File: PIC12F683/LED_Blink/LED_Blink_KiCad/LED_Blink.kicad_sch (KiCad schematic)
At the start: 3 parts, among them U1 PIC12F683-xP

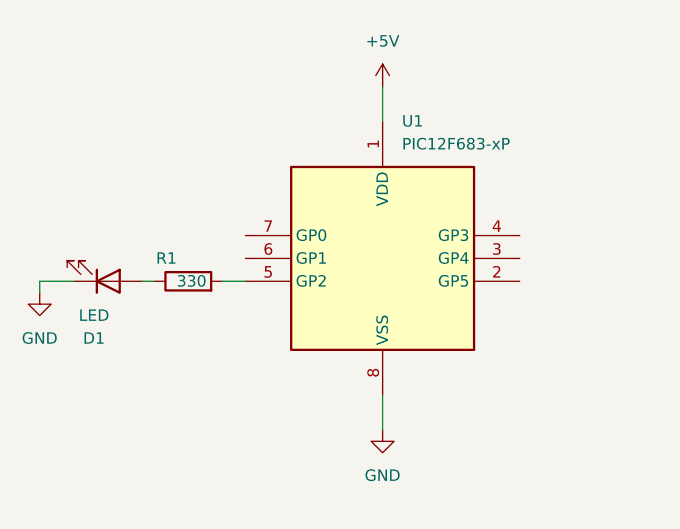
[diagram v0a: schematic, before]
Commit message: Add Capacitor
・Add capacitor
・remove backup file
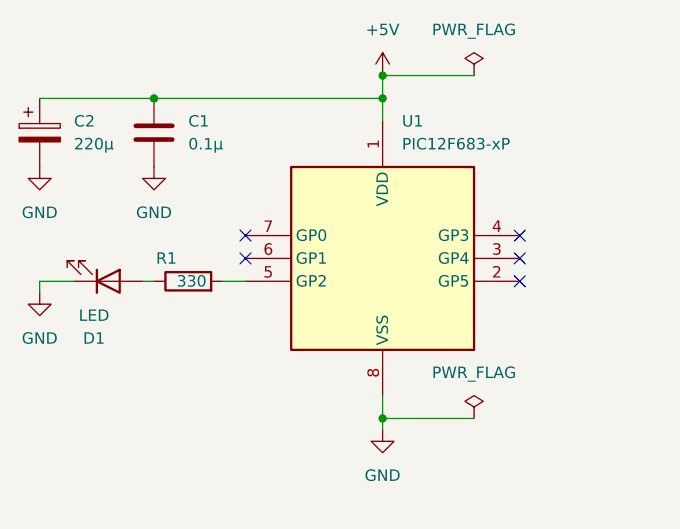
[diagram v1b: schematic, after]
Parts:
- added C1: 0.1μ, Capacitor_THT:C_Disc_D5.0mm_W2.5mm_P2.50mm, symbol Device:C
- added C2: 220μ, Capacitor_THT:CP_Radial_D6.3mm_P2.50mm, symbol Device:C_Polarized
- D1: footprint (none) -> LED_THT:LED_D5.0mm_Horizontal_O1.27mm_Z9.0mm
- R1: footprint (none) -> Resistor_THT:R_Axial_DIN0207_L6.3mm_D2.5mm_P10.16mm_Horizontal
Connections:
- net +5V: now also C1.1, C2.1
- net GND: now also C1.2, C2.2
- no-connect marks 0 -> 5
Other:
- company: (none) -> hirosuke1214
- title: (none) -> LED Blink

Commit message: add about pullup
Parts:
- added R2: 10K, symbol Device:R
- D1: footprint LED_THT:LED_D5.0mm_Horizontal_O1.27mm_Z9.0mm -> (none)
- R1: footprint Resistor_THT:R_Axial_DIN0207_L6.3mm_D2.5mm_P10.16mm_Horizontal -> (none)
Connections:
- net +5V: now also R2.1
- net at D1.2 (A): now also R1.2; no longer R1.1
- net at U1.5 (GP2): now also R1.1; no longer R1.2
- net at U1.4 (GP3): now also R2.2
- no-connect marks 5 -> 4
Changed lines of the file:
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@@
 		(at 127 87.63)
 	)
-	(no_connect
-		(at 157.48 87.63)
-	)
 	(wire
 		(pts
@@
 	(wire
 		(pts
-			(xy 142.24 109.22) (xy 142.24 107.95)
+			(xy 142.24 111.76) (xy 142.24 107.95)
+		)
+		(stroke
+			(width 0)
+			(type default)
+		)
+	)
+	(wire
+		(pts
+			(xy 116.84 109.22) (xy 116.84 111.76)
 		)
 		(stroke
@@
 	(wire
 		(pts
+			(xy 166.37 87.63) (xy 157.48 87.63)
+		)
+		(stroke
+			(width 0)
+			(type default)
+		)
+	)
+	(wire
+		(pts
 			(xy 142.24 69.85) (xy 152.4 69.85)
 		)
@@
 	(wire
 		(pts
-			(xy 115.57 92.71) (xy 116.84 92.71)
-		)
-		(stroke
-			(width 0)
-			(type default)
-		)
-	)
-	(wire
-		(pts
 			(xy 142.24 107.95) (xy 152.4 107.95)
 		)
@@
 	(wire
 		(pts
-			(xy 104.14 92.71) (xy 107.95 92.71)
-		)
-		(stroke
-			(width 0)
-			(type default)
-		)
-	)
-	(wire
-		(pts
-			(xy 124.46 92.71) (xy 127 92.71)
-		)
-		(stroke
-			(width 0)
-			(type default)
-		)
-	)
-	(wire
-		(pts
-			(xy 104.14 93.98) (xy 104.14 92.71)
-		)
-		(stroke
-			(width 0)
-			(type default)
-		)
-	)
-	(symbol
-		(lib_id "Device:R")
-		(at 120.65 92.71 90)
-		(unit 1)
-		(exclude_from_sim no)
-		(in_bom yes)
-		(on_board yes)
-		(dnp no)
-		(property "Reference" "R1"
-			(at 119.3799 90.17 90)
-			(effects
-				(font
-					(size 1.27 1.27)
-				)
-				(justify left)
-			)
-		)
-		(property "Value" "330"
-			(at 122.682 92.71 90)
-			(effects
-				(font
-					(size 1.27 1.27)
-				)
-				(justify left)
-			)
-		)
-		(property "Footprint" "Resistor_THT:R_Axial_DIN0207_L6.3mm_D2.5mm_P10.16mm_Horizontal"
-			(at 120.65 94.488 90)
+			(xy 116.84 92.71) (xy 127 92.71)
+		)
+		(stroke
+			(width 0)
+			(type default)
+		)
+	)
+	(wire
+		(pts
+			(xy 142.24 72.39) (xy 166.37 72.39)
+		)
+		(stroke
+			(width 0)
+			(type default)
+		)
+	)
+	(wire
+		(pts
+			(xy 166.37 80.01) (xy 166.37 87.63)
+		)
+		(stroke
+			(width 0)
+			(type default)
+		)
+	)
+	(wire
+		(pts
+			(xy 116.84 100.33) (xy 116.84 101.6)
+		)
+		(stroke
+			(width 0)
+			(type default)
+		)
+	)
+	(symbol
+		(lib_id "Device:LED")
+		(at 116.84 105.41 90)
+		(unit 1)
+		(exclude_from_sim no)
+		(in_bom yes)
+		(on_board yes)
+		(dnp no)
+		(fields_autoplaced yes)
+		(property "Reference" "D1"
+			(at 120.65 105.7274 90)
+			(effects
+				(font
+					(size 1.27 1.27)
+				)
+				(justify right)
+			)
+		)
+		(property "Value" "LED"
+			(at 120.65 108.2674 90)
+			(effects
+				(font
+					(size 1.27 1.27)
+				)
+				(justify right)
+			)
+		)
+		(property "Footprint" ""
+			(at 116.84 105.41 0)
 			(effects
 				(font
@@
 		)
 		(property "Datasheet" "~"
-			(at 120.65 92.71 0)
-			(effects
-				(font
-					(size 1.27 1.27)
-				)
-				(hide yes)
-			)
-		)
-		(property "Description" "Resistor"
-			(at 120.65 92.71 0)
+			(at 116.84 105.41 0)
+			(effects
+				(font
+					(size 1.27 1.27)
+				)
+				(hide yes)
+			)
+		)
+		(property "Description" "Light emitting diode"
+			(at 116.84 105.41 0)
+			(effects
+				(font
+					(size 1.27 1.27)
+				)
+				(hide yes)
+			)
+		)
+		(property "Sim.Pins" "1=K 2=A"
+			(at 116.84 105.41 0)
 			(effects
 				(font
@@
 			(project ""
 				(path "/fc138699-1ddf-4429-8edd-11ce583ead16"
-					(reference "R1")
+					(reference "D1")
 					(unit 1)
 				)
@@
 	(symbol
 		(lib_id "power:GND")
-		(at 142.24 109.22 0)
+		(at 142.24 111.76 0)
 		(unit 1)
 		(exclude_from_sim no)
@@
 		(fields_autoplaced yes)
 		(property "Reference" "#PWR02"
-			(at 142.24 115.57 0)
+			(at 142.24 118.11 0)
 			(effects
 				(font
@@
 		)
 		(property "Value" "GND"
-			(at 142.24 114.3 0)
+			(at 142.24 116.84 0)
 			(effects
 				(font
@@
 		)
 		(property "Footprint" ""
-			(at 142.24 109.22 0)
+			(at 142.24 111.76 0)
 			(effects
 				(font
@@
 		)
 		(property "Datasheet" ""
-			(at 142.24 109.22 0)
+			(at 142.24 111.76 0)
 			(effects
 				(font
@@
 		)
 		(property "Description" "Power symbol creates a global label with name \"GND\" , ground"
-			(at 142.24 109.22 0)
+			(at 142.24 111.76 0)
 			(effects
 				(font
@@
 	)
 	(symbol
-		(lib_id "Device:LED")
-		(at 111.76 92.71 0)
-		(mirror x)
-		(unit 1)
-		(exclude_from_sim no)
-		(in_bom yes)
-		(on_board yes)
-		(dnp no)
-		(fields_autoplaced yes)
-		(property "Reference" "D1"
-			(at 110.1725 99.06 0)
-			(effects
-				(font
-					(size 1.27 1.27)
-				)
-			)
-		)
-		(property "Value" "LED"
-			(at 110.1725 96.52 0)
-			(effects
-				(font
-					(size 1.27 1.27)
-				)
-			)
-		)
-		(property "Footprint" "LED_THT:LED_D5.0mm_Horizontal_O1.27mm_Z9.0mm"
-			(at 111.76 92.71 0)
+		(lib_id "Device:R")
+		(at 166.37 76.2 0)
+		(unit 1)
+		(exclude_from_sim no)
+		(in_bom yes)
+		(on_board yes)
+		(dnp no)
+		(fields_autoplaced yes)
+		(property "Reference" "R2"
+			(at 168.91 74.9299 0)
+			(effects
+				(font
+					(size 1.27 1.27)
+				)
+				(justify left)
+			)
+		)
+		(property "Value" "10K"
+			(at 168.91 77.4699 0)
+			(effects
+				(font
+					(size 1.27 1.27)
+				)
+				(justify left)
+			)
+		)
+		(property "Footprint" ""
+			(at 164.592 76.2 90)
 			(effects
 				(font
@@
 		)
 		(property "Datasheet" "~"
-			(at 111.76 92.71 0)
-			(effects
-				(font
-					(size 1.27 1.27)
-				)
-				(hide yes)
-			)
-		)
-		(property "Description" "Light emitting diode"
-			(at 111.76 92.71 0)
-			(effects
-				(font
-					(size 1.27 1.27)
-				)
-				(hide yes)
-			)
-		)
-		(property "Sim.Pins" "1=K 2=A"
-			(at 111.76 92.71 0)
+			(at 166.37 76.2 0)
+			(effects
+				(font
+					(size 1.27 1.27)
+				)
+				(hide yes)
+			)
+		)
+		(property "Description" "Resistor"
+			(at 166.37 76.2 0)
 			(effects
 				(font
@@
 			(project ""
 				(path "/fc138699-1ddf-4429-8edd-11ce583ead16"
-					(reference "D1")
+					(reference "R2")
 					(unit 1)
 				)
@@
 	(symbol
 		(lib_id "power:GND")
-		(at 104.14 93.98 0)
+		(at 116.84 111.76 0)
 		(unit 1)
 		(exclude_from_sim no)
@@
 		(fields_autoplaced yes)
 		(property "Reference" "#PWR03"
-			(at 104.14 100.33 0)
+			(at 116.84 118.11 0)
 			(effects
 				(font
@@
 		)
 		(property "Value" "GND"
-			(at 104.14 99.06 0)
+			(at 116.84 116.84 0)
 			(effects
 				(font
@@
 		)
 		(property "Footprint" ""
-			(at 104.14 93.98 0)
+			(at 116.84 111.76 0)
 			(effects
 				(font
@@
 		)
 		(property "Datasheet" ""
-			(at 104.14 93.98 0)
+			(at 116.84 111.76 0)
 			(effects
 				(font
@@
 		)
 		(property "Description" "Power symbol creates a global label with name \"GND\" , ground"
-			(at 104.14 93.98 0)
+			(at 116.84 111.76 0)
 			(effects
 				(font
@@
 					(unit 1)
 				)
+			)
+		)
+	)
+	(symbol
+		(lib_id "Device:R")
+		(at 116.84 96.52 0)
+		(unit 1)
+		(exclude_from_sim no)
+		(in_bom yes)
+		(on_board yes)
+		(dnp no)
+		(fields_autoplaced yes)
+		(property "Reference" "R1"
+			(at 119.38 95.2499 0)
+			(effects
+				(font
+					(size 1.27 1.27)
+				)
+				(justify left)
+			)
+		)
+		(property "Value" "330"
+			(at 119.38 97.7899 0)
+			(effects
+				(font
+					(size 1.27 1.27)
+				)
+				(justify left)
+			)
+		)
+		(property "Footprint" ""
+			(at 115.062 96.52 90)
+			(effects
+				(font
+					(size 1.27 1.27)
+				)
+				(hide yes)
+			)
+		)
+		(property "Datasheet" "~"
+			(at 116.84 96.52 0)
+			(effects
+				(font
+					(size 1.27 1.27)
+				)
+				(hide yes)
+			)
+		)
+		(property "Description" "Resistor"
+			(at 116.84 96.52 0)
+			(effects
+				(font
+					(size 1.27 1.27)
+				)
+				(hide yes)
+			)
+		)
+		(pin "2"
+		)
+		(pin "1"
+		)
+		(instances
+			(project ""
+				(path "/fc138699-1ddf-4429-8edd-11ce583ead16"
+					(reference "R1")
+					(unit 1)
+				)

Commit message: update image and circuit diagram
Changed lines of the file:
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@@
-	)
-	(junction
-		(at 142.24 107.95)
-		(diameter 0)
-		(color 0 0 0 0)
-	)
-	(junction
-		(at 142.24 69.85)
-		(diameter 0)
-		(color 0 0 0 0)
 	)
 	(junction
@@
 	(wire
 		(pts
-			(xy 142.24 111.76) (xy 142.24 107.95)
+			(xy 142.24 105.41) (xy 142.24 111.76)
 		)
 		(stroke
@@
 	(wire
 		(pts
-			(xy 142.24 69.85) (xy 152.4 69.85)
-		)
-		(stroke
-			(width 0)
-			(type default)
-		)
-	)
-	(wire
-		(pts
 			(xy 104.14 72.39) (xy 116.84 72.39)
 		)
@@
 		(pts
 			(xy 116.84 72.39) (xy 142.24 72.39)
-		)
-		(stroke
-			(width 0)
-			(type default)
-		)
-	)
-	(wire
-		(pts
-			(xy 142.24 107.95) (xy 152.4 107.95)
-		)
-		(stroke
-			(width 0)
-			(type default)
-		)
-	)
-	(wire
-		(pts
-			(xy 142.24 105.41) (xy 142.24 107.95)
 		)
 		(stroke
@@
 	)
 	(symbol
-		(lib_id "power:PWR_FLAG")
-		(at 152.4 69.85 0)
-		(unit 1)
-		(exclude_from_sim no)
-		(in_bom yes)
-		(on_board yes)
-		(dnp no)
-		(fields_autoplaced yes)
-		(property "Reference" "#FLG01"
-			(at 152.4 67.945 0)
-			(effects
-				(font
-					(size 1.27 1.27)
-				)
-				(hide yes)
-			)
-		)
-		(property "Value" "PWR_FLAG"
-			(at 152.4 64.77 0)
-			(effects
-				(font
-					(size 1.27 1.27)
-				)
-			)
-		)
-		(property "Footprint" ""
-			(at 152.4 69.85 0)
-			(effects
-				(font
-					(size 1.27 1.27)
-				)
-				(hide yes)
-			)
-		)
-		(property "Datasheet" "~"
-			(at 152.4 69.85 0)
-			(effects
-				(font
-					(size 1.27 1.27)
-				)
-				(hide yes)
-			)
-		)
-		(property "Description" "Special symbol for telling ERC where power comes from"
-			(at 152.4 69.85 0)
-			(effects
-				(font
-					(size 1.27 1.27)
-				)
-				(hide yes)
-			)
-		)
-		(pin "1"
-		)
-		(instances
-			(project ""
-				(path "/fc138699-1ddf-4429-8edd-11ce583ead16"
-					(reference "#FLG01")
-					(unit 1)
-				)
-			)
-		)
-	)
-	(symbol
 		(lib_id "power:GND")
 		(at 104.14 80.01 0)
@@
 					(unit 1)
 				)
-			)
-		)
-	)
-	(symbol
-		(lib_id "power:PWR_FLAG")
-		(at 152.4 107.95 0)
-		(unit 1)
-		(exclude_from_sim no)
-		(in_bom yes)
-		(on_board yes)
-		(dnp no)
-		(fields_autoplaced yes)
-		(property "Reference" "#FLG02"
-			(at 152.4 106.045 0)
-			(effects
-				(font
-					(size 1.27 1.27)
-				)
-				(hide yes)
-			)
-		)
-		(property "Value" "PWR_FLAG"
-			(at 152.4 102.87 0)
-			(effects
-				(font
-					(size 1.27 1.27)
-				)
-			)
-		)
-		(property "Footprint" ""
-			(at 152.4 107.95 0)
-			(effects
-				(font
-					(size 1.27 1.27)
-				)
-				(hide yes)
-			)
-		)
-		(property "Datasheet" "~"
-			(at 152.4 107.95 0)
-			(effects
-				(font
-					(size 1.27 1.27)
-				)
-				(hide yes)
-			)
-		)
-		(property "Description" "Special symbol for telling ERC where power comes from"
-			(at 152.4 107.95 0)
-			(effects
-				(font
-					(size 1.27 1.27)
-				)
-				(hide yes)
-			)
-		)
-		(pin "1"
-		)
-		(instances
-			(project "LED_Blink"
-				(path "/fc138699-1ddf-4429-8edd-11ce583ead16"
-					(reference "#FLG02")
-					(unit 1)
-				)
